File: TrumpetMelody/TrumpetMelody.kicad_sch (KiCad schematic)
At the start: 80 parts, among them J1 USB_B_Micro, J2 Conn_01x05, J3 640456-3, J4 640456-3, SW1 SW_Push, U1 STM32F411RETx, U2 TLV62565DBVR, U3 MAX98357AETE_T, U4 MAX7375AXR805

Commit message: Updated TVS Diodes to be right size and fixed placements
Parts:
- D1, D2, D3, D4, D5, D6: footprint Diode_SMD:D_01005_0402Metric_Pad0.57x0.30mm_HandSolder -> Diode_SMD:D_0805_2012Metric
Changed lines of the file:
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@@
       (effects (font (size 1.27 1.27)) (justify right))
     )
-    (property "Footprint" "Diode_SMD:D_01005_0402Metric_Pad0.57x0.30mm_HandSolder" (at 265.43 102.87 0)
+    (property "Footprint" "Diode_SMD:D_0805_2012Metric" (at 265.43 102.87 0)
       (effects (font (size 1.27 1.27)) hide)
     )
@@
       (effects (font (size 1.27 1.27)) (justify right))
     )
-    (property "Footprint" "Diode_SMD:D_01005_0402Metric_Pad0.57x0.30mm_HandSolder" (at 377.19 231.14 0)
+    (property "Footprint" "Diode_SMD:D_0805_2012Metric" (at 377.19 231.14 0)
       (effects (font (size 1.27 1.27)) hide)
     )
@@
       (effects (font (size 1.27 1.27)) (justify right))
     )
-    (property "Footprint" "Diode_SMD:D_01005_0402Metric_Pad0.57x0.30mm_HandSolder" (at 292.1 102.87 0)
+    (property "Footprint" "Diode_SMD:D_0805_2012Metric" (at 292.1 102.87 0)
       (effects (font (size 1.27 1.27)) hide)
     )
@@
       (effects (font (size 1.27 1.27)) (justify right))
     )
-    (property "Footprint" "Diode_SMD:D_01005_0402Metric_Pad0.57x0.30mm_HandSolder" (at 302.26 160.02 0)
+    (property "Footprint" "Diode_SMD:D_0805_2012Metric" (at 302.26 160.02 0)
       (effects (font (size 1.27 1.27)) hide)
     )
@@
       (effects (font (size 1.27 1.27)) (justify right))
     )
-    (property "Footprint" "Diode_SMD:D_01005_0402Metric_Pad0.57x0.30mm_HandSolder" (at 215.9 231.14 0)
+    (property "Footprint" "Diode_SMD:D_0805_2012Metric" (at 215.9 231.14 0)
       (effects (font (size 1.27 1.27)) hide)
     )
@@
       (effects (font (size 1.27 1.27)) (justify right))
     )
-    (property "Footprint" "Diode_SMD:D_01005_0402Metric_Pad0.57x0.30mm_HandSolder" (at 294.64 231.14 0)
-      (effects (font (size 1.27 1.27)) hide)
-    )
+    (property "Footprint" "Diode_SMD:D_0805_2012Metric" (at 294.64 231.14 0)
+      (effects (font (size 1.27 1.27)) hide)
+    )

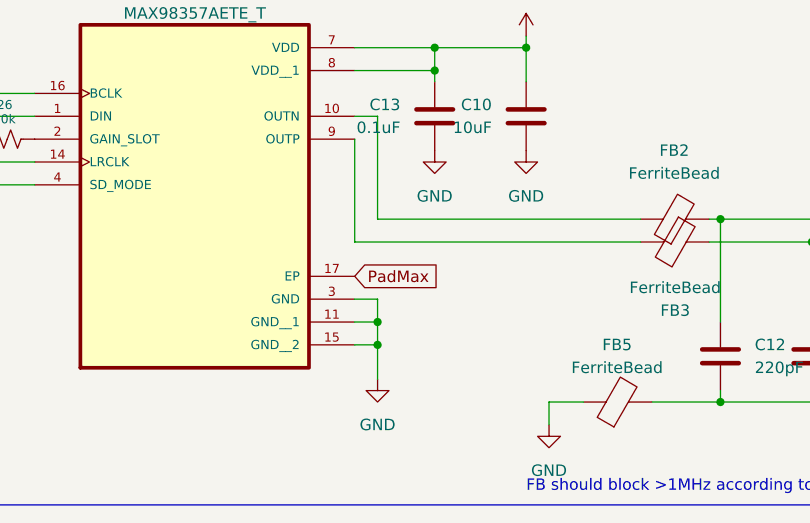
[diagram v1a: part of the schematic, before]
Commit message: Added a bunch of ground planes
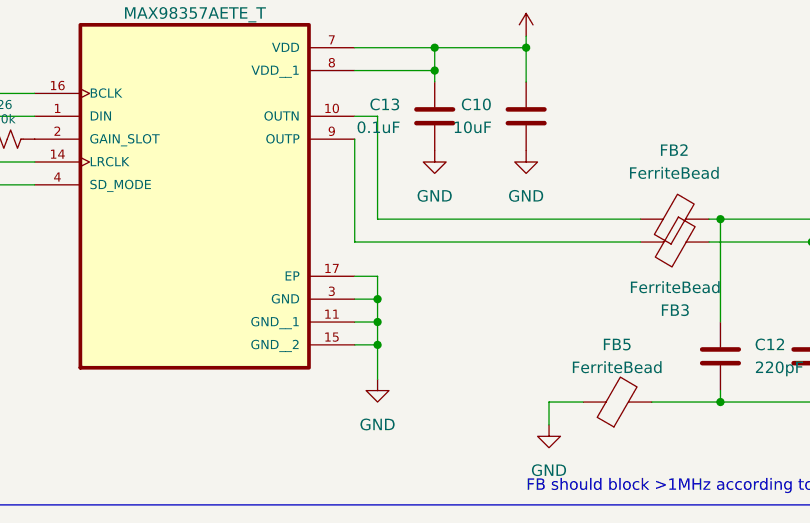
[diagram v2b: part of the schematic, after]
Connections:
- net PadMax is gone; now on net GND: U3.17 (EP)
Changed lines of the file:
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@@
   (junction (at 265.43 95.25) (diameter 0) (color 0 0 0 0)
   )
+  (junction (at 83.82 251.46) (diameter 0) (color 0 0 0 0)
+  )
   (junction (at 254 260.35) (diameter 0) (color 0 0 0 0)
   )
@@
     (stroke (width 0) (type default))
   )
+  (wire (pts (xy 83.82 248.92) (xy 83.82 251.46))
+    (stroke (width 0) (type default))
+  )
   (wire (pts (xy 185.42 222.25) (xy 185.42 226.06))
     (stroke (width 0) (type default))
@@
   )
   (wire (pts (xy 83.82 260.35) (xy 83.82 256.54))
+    (stroke (width 0) (type default))
+  )
+  (wire (pts (xy 81.28 248.92) (xy 83.82 248.92))
     (stroke (width 0) (type default))
   )
@@
     )
   )
-  (global_label "PadMax" (shape input) (at 81.28 248.92 0) (fields_autoplaced)
-    (effects (font (size 1.27 1.27)) (justify left))
-    (property "Intersheetrefs" "${INTERSHEET_REFS}" (at 90.7281 248.92 0)
-      (effects (font (size 1.27 1.27)) (justify left) hide)
-    )
-  )

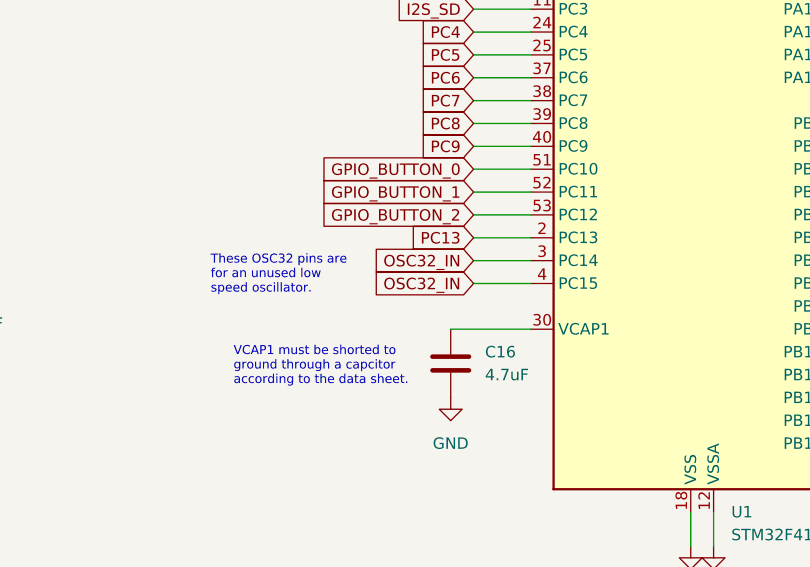
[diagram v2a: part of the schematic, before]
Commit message: Pulled out most of the GPIO pins to vias
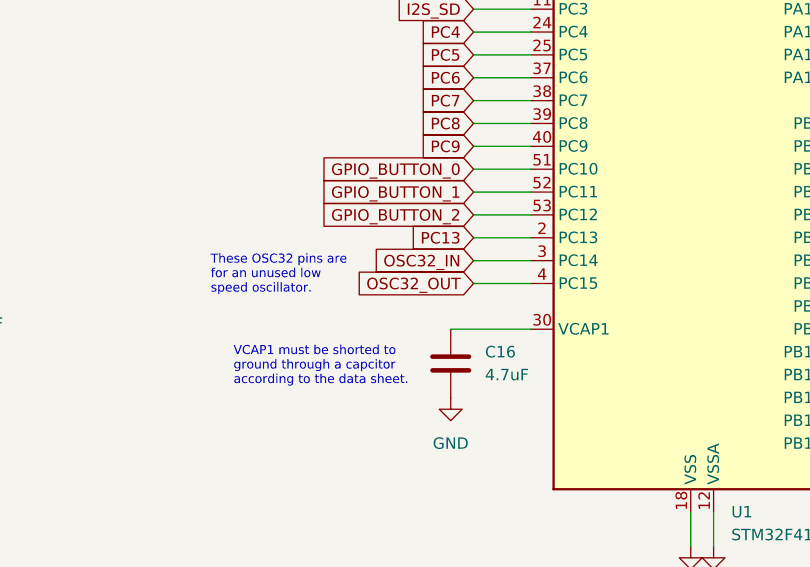
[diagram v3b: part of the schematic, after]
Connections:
- net OSC32_IN: no longer U1.4 (PC15)
- new net OSC32_OUT: U1.4 (PC15)
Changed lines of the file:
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@@
     )
   )
-  (global_label "OSC32_IN" (shape input) (at 132.08 166.37 180) (fields_autoplaced)
+  (global_label "OSC32_OUT" (shape input) (at 132.08 166.37 180) (fields_autoplaced)
     (effects (font (size 1.27 1.27)) (justify right))
-    (property "Intersheetrefs" "${INTERSHEET_REFS}" (at 120.6171 166.37 0)
+    (property "Intersheetrefs" "${INTERSHEET_REFS}" (at 119.0032 166.37 0)
       (effects (font (size 1.27 1.27)) (justify right) hide)
     )

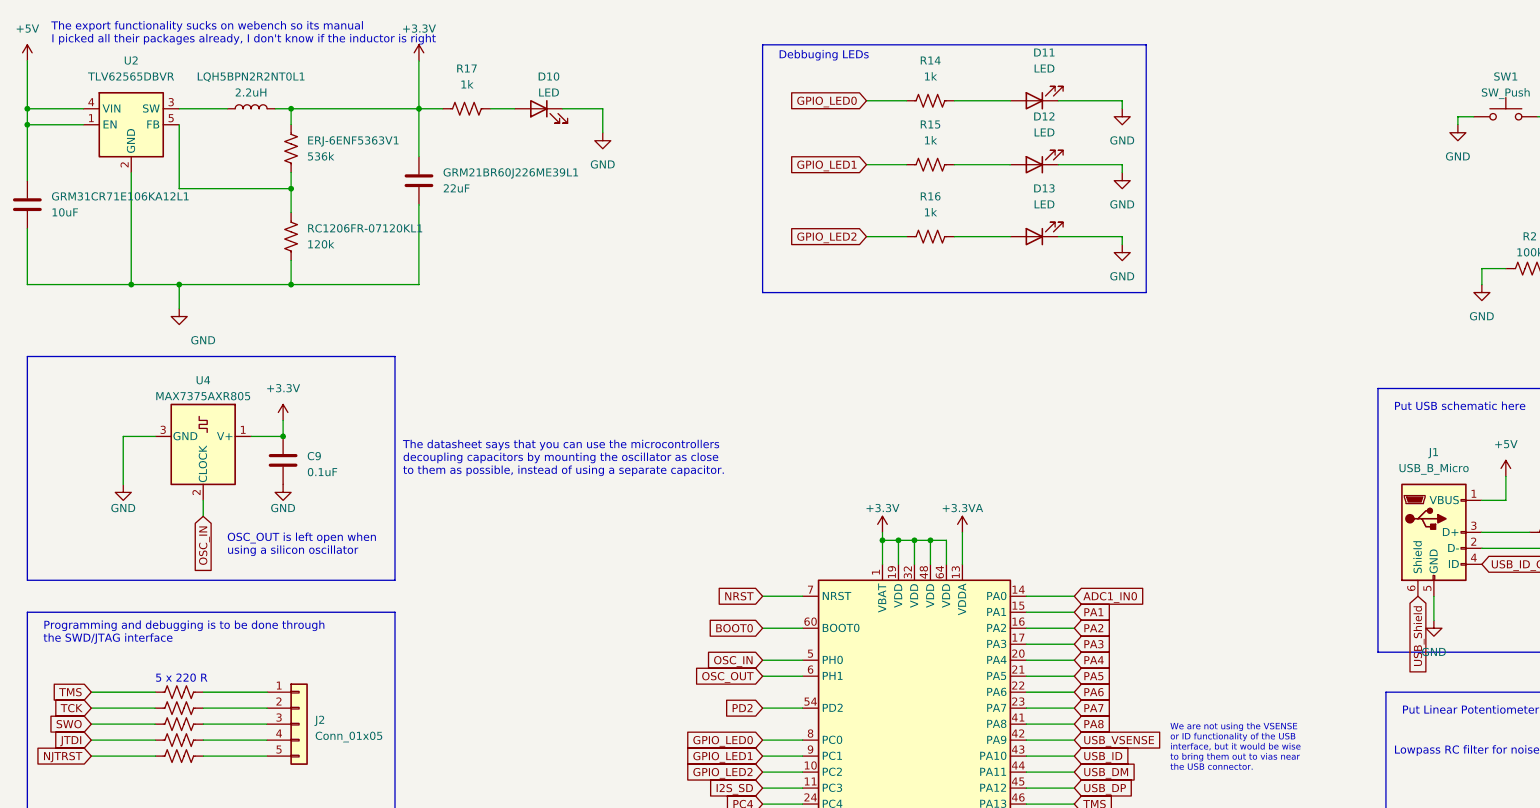
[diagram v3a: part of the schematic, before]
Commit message: Fixed DRC errors
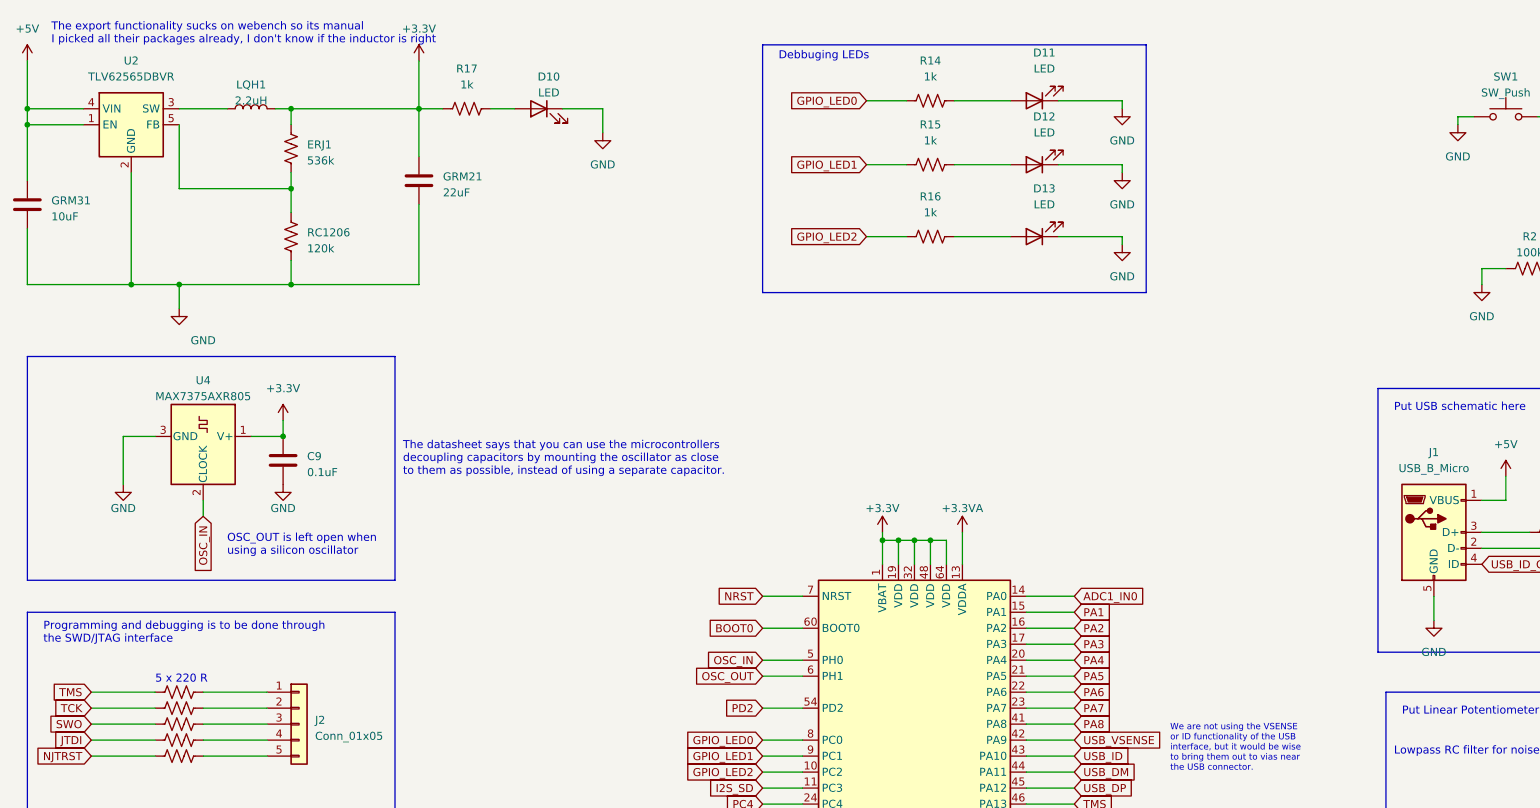
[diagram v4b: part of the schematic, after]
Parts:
- U3: footprint TrumpetMelodyFootprintLibrary:QFN50P300X300X80-17N -> TrumpetMelodyFootprintLibrary:21-0136I_T1633-4_MXM-M
- renumbered ERJ-6ENF5363V1 to ERJ1, GRM21BR60J226ME39L1 to GRM21, GRM31CR71E106KA12L1 to GRM31, LQH5BPN2R2NT0L1 to LQH1, RC1206FR-07120KL1 to RC1206
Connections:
- removed net USB_Shield: J1.6 (Shield)
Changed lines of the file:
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@@
-    )
-  )
-  (global_label "USB_Shield" (shape input) (at 236.22 105.41 270) (fields_autoplaced)
-    (effects (font (size 1.27 1.27)) (justify right))
-    (property "Intersheetrefs" "${INTERSHEET_REFS}" (at 236.22 118.3053 90)
-      (effects (font (size 1.27 1.27)) (justify right) hide)
     )
   )
@@
     (pin "4")
     (pin "5")
-    (pin "6")
     (instances
       (project "TrumpetMelody"
@@
   (symbol (lib_id "Device:R_US") (at 57.15 34.29 0) (unit 1)
     (in_bom yes) (on_board yes) (dnp no) (fields_autoplaced)
-    (property "Reference" "ERJ-6ENF5363V1" (at 59.69 33.02 0)
-      (effects (font (size 1.27 1.27)) (justify left))
-    )
-    (property "Value" "536k" (at 59.69 35.56 0)
+    (property "Reference" "ERJ1" (at 59.69 33.655 0)
+      (effects (font (size 1.27 1.27)) (justify left))
+    )
+    (property "Value" "536k" (at 59.69 36.195 0)
       (effects (font (size 1.27 1.27)) (justify left))
     )
@@
       (project "TrumpetMelody"
         (path "/646bb87a-580f-408c-a344-dec391089cbb"
-          (reference "ERJ-6ENF5363V1") (unit 1)
+          (reference "ERJ1") (unit 1)
         )
       )
@@
   (symbol (lib_id "Device:C") (at 77.47 39.37 0) (unit 1)
     (in_bom yes) (on_board yes) (dnp no) (fields_autoplaced)
-    (property "Reference" "GRM21BR60J226ME39L1" (at 81.28 38.1 0)
-      (effects (font (size 1.27 1.27)) (justify left))
-    )
-    (property "Value" "22uF" (at 81.28 40.64 0)
+    (property "Reference" "GRM21" (at 81.28 38.735 0)
+      (effects (font (size 1.27 1.27)) (justify left))
+    )
+    (property "Value" "22uF" (at 81.28 41.275 0)
       (effects (font (size 1.27 1.27)) (justify left))
     )
@@
       (project "TrumpetMelody"
         (path "/646bb87a-580f-408c-a344-dec391089cbb"
-          (reference "GRM21BR60J226ME39L1") (unit 1)
+          (reference "GRM21") (unit 1)
         )
       )
@@
   (symbol (lib_id "Device:C") (at 15.24 43.18 0) (unit 1)
     (in_bom yes) (on_board yes) (dnp no) (fields_autoplaced)
-    (property "Reference" "GRM31CR71E106KA12L1" (at 19.05 41.91 0)
-      (effects (font (size 1.27 1.27)) (justify left))
-    )
-    (property "Value" "10uF" (at 19.05 44.45 0)
+    (property "Reference" "GRM31" (at 19.05 42.545 0)
+      (effects (font (size 1.27 1.27)) (justify left))
+    )
+    (property "Value" "10uF" (at 19.05 45.085 0)
       (effects (font (size 1.27 1.27)) (justify left))
     )
@@
       (project "TrumpetMelody"
         (path "/646bb87a-580f-408c-a344-dec391089cbb"
-          (reference "GRM31CR71E106KA12L1") (unit 1)
+          (reference "GRM31") (unit 1)
         )
       )
@@
   (symbol (lib_id "Device:L") (at 50.8 27.94 90) (unit 1)
     (in_bom yes) (on_board yes) (dnp no) (fields_autoplaced)
-    (property "Reference" "LQH5BPN2R2NT0L1" (at 50.8 22.86 90)
-      (effects (font (size 1.27 1.27)))
-    )
-    (property "Value" "2.2uH" (at 50.8 25.4 90)
+    (property "Reference" "LQH1" (at 50.8 24.13 90)
+      (effects (font (size 1.27 1.27)))
+    )
+    (property "Value" "2.2uH" (at 50.8 26.67 90)
       (effects (font (size 1.27 1.27)))
     )
@@
       (project "TrumpetMelody"
         (path "/646bb87a-580f-408c-a344-dec391089cbb"
-          (reference "LQH5BPN2R2NT0L1") (unit 1)
+          (reference "LQH1") (unit 1)
         )
       )
@@
       (effects (font (size 1.27 1.27)))
     )
-    (property "Footprint" "TrumpetMelodyFootprintLibrary:QFN50P300X300X80-17N" (at 63.5 236.22 0)
+    (property "Footprint" "TrumpetMelodyFootprintLibrary:21-0136I_T1633-4_MXM-M" (at 63.5 236.22 0)
       (effects (font (size 1.27 1.27)) (justify bottom) hide)
     )
@@
   (symbol (lib_id "Device:R_US") (at 57.15 48.26 0) (unit 1)
     (in_bom yes) (on_board yes) (dnp no) (fields_autoplaced)
-    (property "Reference" "RC1206FR-07120KL1" (at 59.69 46.99 0)
-      (effects (font (size 1.27 1.27)) (justify left))
-    )
-    (property "Value" "120k" (at 59.69 49.53 0)
+    (property "Reference" "RC1206" (at 59.69 47.625 0)
+      (effects (font (size 1.27 1.27)) (justify left))
+    )
+    (property "Value" "120k" (at 59.69 50.165 0)
       (effects (font (size 1.27 1.27)) (justify left))
     )
@@
       (project "TrumpetMelody"
         (path "/646bb87a-580f-408c-a344-dec391089cbb"
-          (reference "RC1206FR-07120KL1") (unit 1)
-        )
-      )
+          (reference "RC1206") (unit 1)
+        )
+      )
